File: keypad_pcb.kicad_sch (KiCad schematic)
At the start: 8 parts

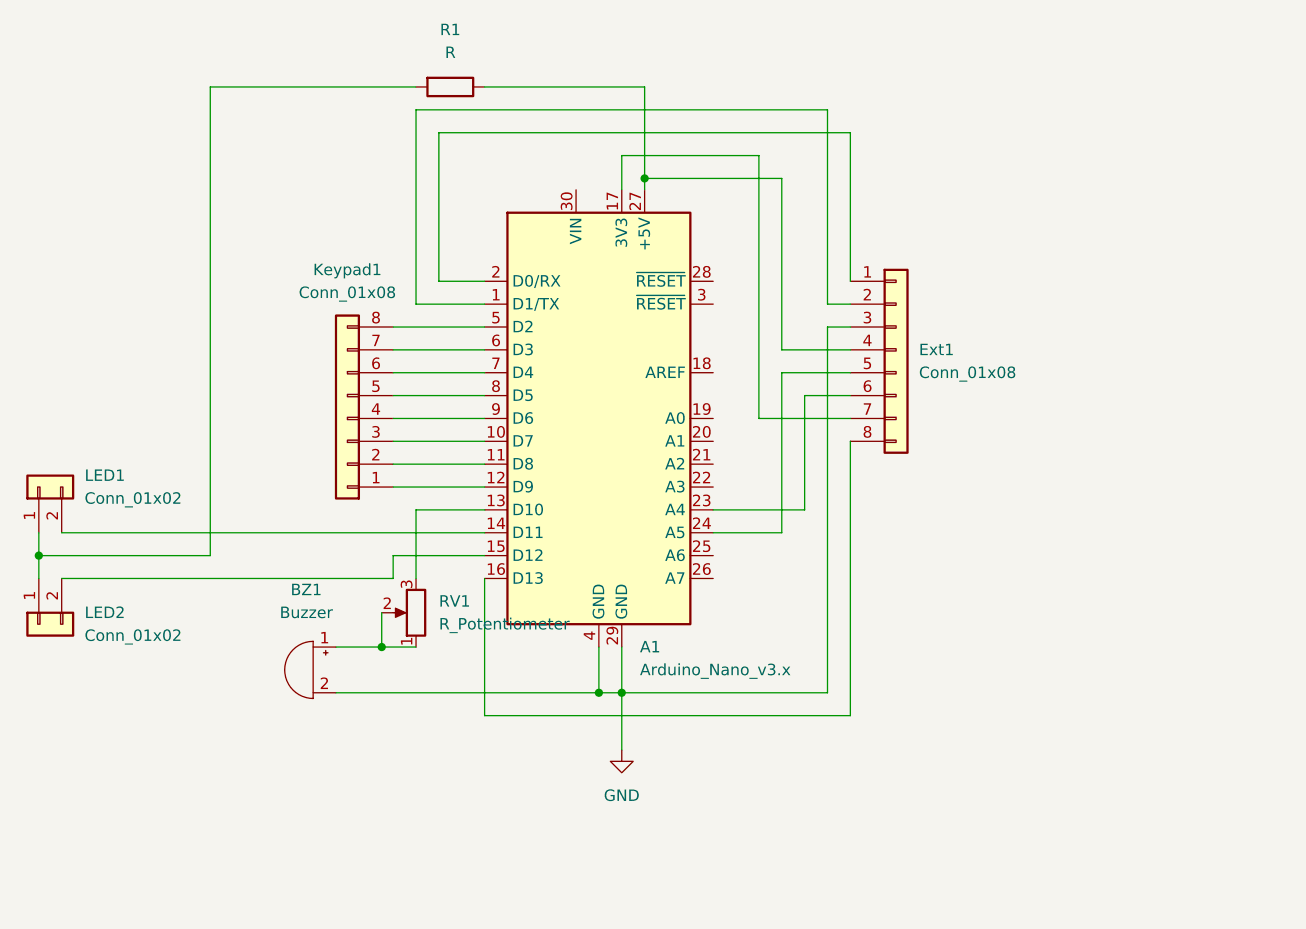
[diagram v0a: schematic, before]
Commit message: Rework for Arduino Pro Micro
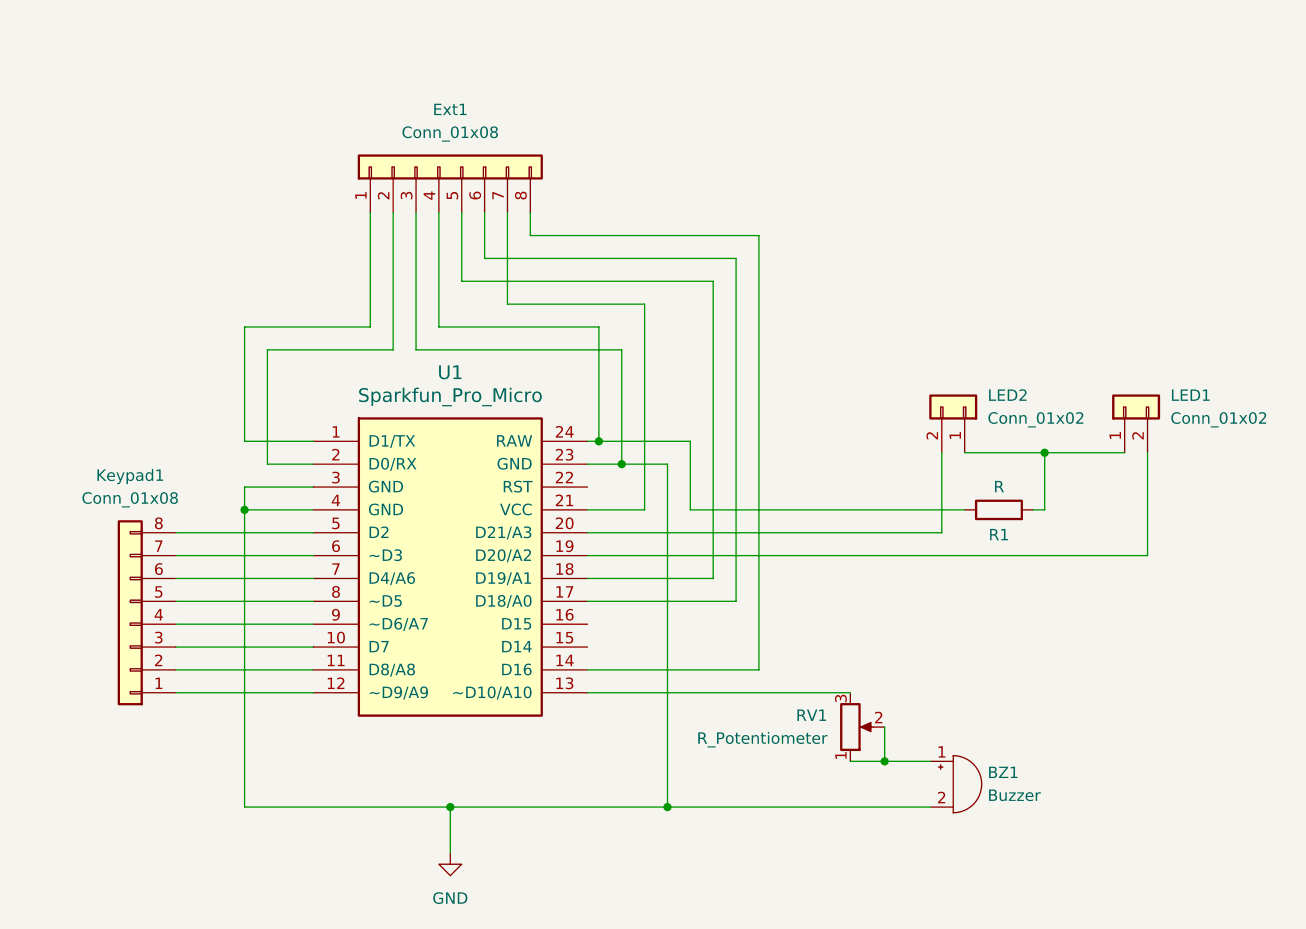
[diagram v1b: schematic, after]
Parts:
- removed A1: Arduino_Nano_v3.x, Module:Arduino_Nano, symbol MCU_Module:Arduino_Nano_v3.x
- added U1: Sparkfun_Pro_Micro, Arduino:Sparkfun_Pro_Micro, symbol Arduino:Sparkfun_Pro_Micro
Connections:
- net GND: now also U1.23 (GND), U1.3 (GND), U1.4 (GND)
- net at Ext1.4 (Pin_4), R1.1: now also U1.24 (RAW)
- net at Keypad1.1 (Pin_1): now also U1.12 (~D9/A9)
- net at Keypad1.2 (Pin_2): now also U1.11 (D8/A8)
- net at Keypad1.3 (Pin_3): now also U1.10 (D7)
- net at Keypad1.4 (Pin_4): now also U1.9 (~D6/A7)
- net at Keypad1.5 (Pin_5): now also U1.8 (~D5)
- net at Keypad1.6 (Pin_6): now also U1.7 (D4/A6)
- net at Keypad1.7 (Pin_7): now also U1.6 (~D3)
- net at Keypad1.8 (Pin_8): now also U1.5 (D2)
- net at Ext1.1 (Pin_1): now also U1.1 (D1/TX)
- net at Ext1.2 (Pin_2): now also U1.2 (D0/RX)
- net at Ext1.5 (Pin_5): now also U1.18 (D19/A1)
- net at Ext1.6 (Pin_6): now also U1.17 (D18/A0)
- net at Ext1.7 (Pin_7): now also U1.21 (VCC)
- net at Ext1.8 (Pin_8): now also U1.14 (D16)
- net at RV1.3: now also U1.13 (~D10/A10)
- net at LED1.2 (Pin_2): now also U1.19 (D20/A2)
- net at LED2.2 (Pin_2): now also U1.20 (D21/A3)
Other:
- company: (none) -> Mathieu Abati
- title: (none) -> Alarm keypad

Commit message: Update potentiometer to add PCB hole and integrate 3D shape
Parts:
- RV1: footprint Potentiometer_THT:Potentiometer_Piher_PT-10-V10_Vertical -> Potentiometer_THT:Potentiometer_Piher_PT-10-V10_Vertical_Hole
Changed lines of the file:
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@@
 			)
 		)
-		(property "Footprint" "Potentiometer_THT:Potentiometer_Piher_PT-10-V10_Vertical"
+		(property "Footprint" "Potentiometer_THT:Potentiometer_Piher_PT-10-V10_Vertical_Hole"
 			(at 171.45 125.73 0)
 			(effects
